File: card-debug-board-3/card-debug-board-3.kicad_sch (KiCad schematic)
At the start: 98 parts, among them J1 USB4105-GF-A, J2 USB4105-GF-A, J3 Conn_01x05, J4 5040501291, J5 2-1734592-0, Q1 PMV450ENEAR, Q2 PMV450ENEAR, Q3 NTR4101P, SW1 B3F-1000, SW2 PCM13SMTR, SW3 B3F-1000, SW4 SW_DIP_x01, U1 MIC5205-3.3YM5, U2 W25Q16JVSS, U3 RP2040, U4 74AUP1G17, U5 74AUP1G17, U6 IP4234CZ6,125, U7 IP4234CZ6,125, Y1 12 MHz

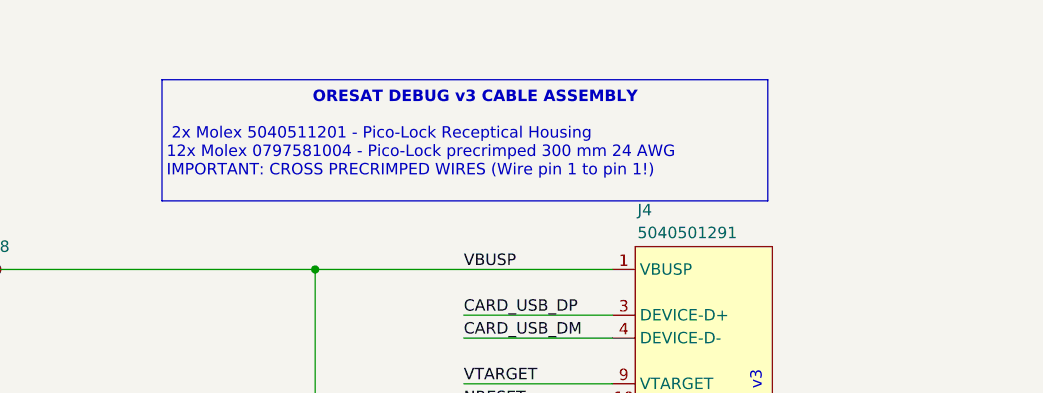
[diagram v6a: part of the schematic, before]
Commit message: Fixed note on card debug v3 cable assembly - it was wrong!
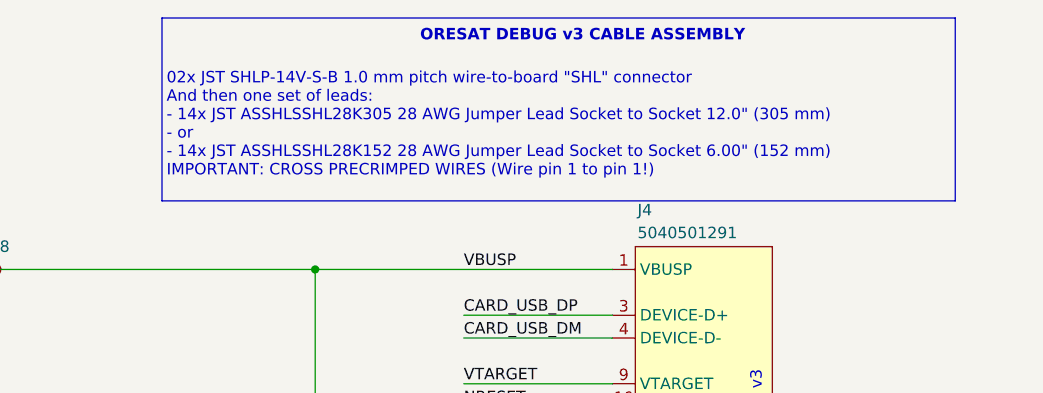
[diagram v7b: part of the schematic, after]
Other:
- note added: "02x JST SHLP-14V-S-B 1.0 mm pitch wire-to-board "SHL" connector And then one set of leads: - 14x JST ASSHLSSHL28K305 28 AWG Jumper Lead Socket to Socket 12.0" (305 mm) - or - 14x JST ASSHLSSHL28K152 28 AWG Jumper Lead Socket to Socket 6.00" (152 mm) IMPORTANT: CROSS PRECRIMPED WIRES (Wire pin 1 to pin 1!)"
- note removed: "2x Molex 5040511201 - Pico-Lock Receptical Housing 12x Molex 0797581004 - Pico-Lock precrimped 300 mm 24 AWG IMPORTANT: CROSS PRECRIMPED WIRES (Wire pin 1 to pin 1!)"
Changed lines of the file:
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@@
 	)
 	(rectangle
-		(start 318.262 25.908)
-		(end 385.572 39.37)
+		(start 318.262 19.05)
+		(end 406.4 39.37)
 		(stroke
 			(width 0)
@@
 		)
 	)
-	(text " 2x Molex 5040511201 - Pico-Lock Receptical Housing\n12x Molex 0797581004 - Pico-Lock precrimped 300 mm 24 AWG\nIMPORTANT: CROSS PRECRIMPED WIRES (Wire pin 1 to pin 1!)"
+	(text "02x JST SHLP-14V-S-B 1.0 mm pitch wire-to-board \"SHL\" connector\nAnd then one set of leads:\n- 14x JST ASSHLSSHL28K305 28 AWG Jumper Lead Socket to Socket 12.0\" (305 mm)\n- or \n- 14x JST ASSHLSSHL28K152 28 AWG Jumper Lead Socket to Socket 6.00\" (152 mm)\nIMPORTANT: CROSS PRECRIMPED WIRES (Wire pin 1 to pin 1!)"
 		(exclude_from_sim no)
 		(at 318.77 36.83 0)
@@
 	(text "ORESAT DEBUG v3 CABLE ASSEMBLY"
 		(exclude_from_sim no)
-		(at 353.06 27.94 0)
+		(at 364.998 21.082 0)
 		(effects
 			(font

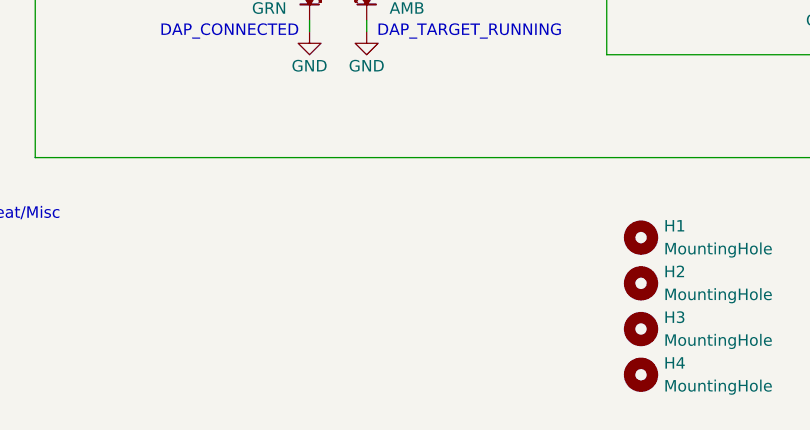
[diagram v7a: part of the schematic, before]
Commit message: Card Debug Board v3.2
Fixed SW2 through-holes which have never been right, added fiducials, added makefile and readmes.
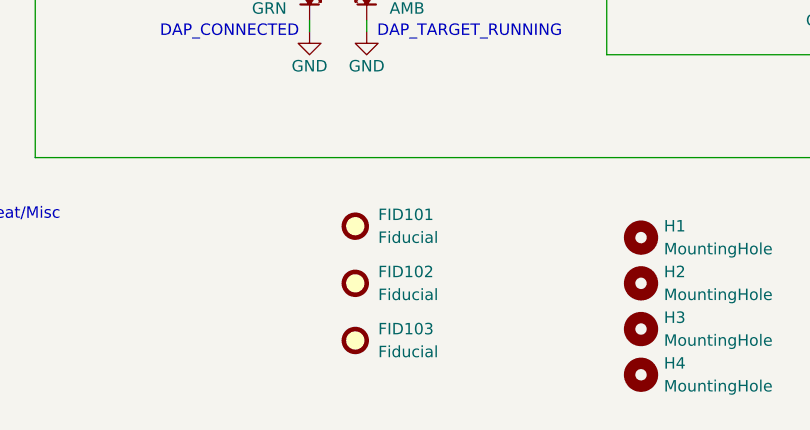
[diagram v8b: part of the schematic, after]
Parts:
- added FID101, FID102, FID103: Fiducial, Fiducial:Fiducial_0.5mm_Mask1mm, symbol Mechanical:Fiducial
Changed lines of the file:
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@@
 	(title_block
 		(title "Card Debug Board")
-		(date "2026-02-08")
-		(rev "3.1")
+		(date "2026-03-11")
+		(rev "3.2")
 		(company "Portland State Aerospace Society")
 	)
@@
 	)
 	(symbol
+		(lib_id "Mechanical:Fiducial")
+		(at 215.9 242.57 0)
+		(unit 1)
+		(exclude_from_sim no)
+		(in_bom no)
+		(on_board yes)
+		(dnp no)
+		(fields_autoplaced yes)
+		(property "Reference" "FID101"
+			(at 218.44 241.2999 0)
+			(effects
+				(font
+					(size 1.27 1.27)
+				)
+				(justify left)
+			)
+		)
+		(property "Value" "Fiducial"
+			(at 218.44 243.8399 0)
+			(effects
+				(font
+					(size 1.27 1.27)
+				)
+				(justify left)
+			)
+		)
+		(property "Footprint" "Fiducial:Fiducial_0.5mm_Mask1mm"
+			(at 215.9 242.57 0)
+			(effects
+				(font
+					(size 1.27 1.27)
+				)
+				(hide yes)
+			)
+		)
+		(property "Datasheet" "~"
+			(at 215.9 242.57 0)
+			(effects
+				(font
+					(size 1.27 1.27)
+				)
+				(hide yes)
+			)
+		)
+		(property "Description" "Fiducial Marker"
+			(at 215.9 242.57 0)
+			(effects
+				(font
+					(size 1.27 1.27)
+				)
+				(hide yes)
+			)
+		)
+		(instances
+			(project ""
+				(path "/6ec99451-f949-47af-a175-ad55f6cf8202"
+					(reference "FID101")
+					(unit 1)
+				)
+			)
+		)
+	)
+	(symbol
 		(lib_id "power:GND")
 		(at 71.12 194.31 0)
@@
 	)
 	(symbol
+		(lib_id "Mechanical:Fiducial")
+		(at 215.9 255.27 0)
+		(unit 1)
+		(exclude_from_sim no)
+		(in_bom no)
+		(on_board yes)
+		(dnp no)
+		(fields_autoplaced yes)
+		(property "Reference" "FID103"
+			(at 218.44 253.9999 0)
+			(effects
+				(font
+					(size 1.27 1.27)
+				)
+				(justify left)
+			)
+		)
+		(property "Value" "Fiducial"
+			(at 218.44 256.5399 0)
+			(effects
+				(font
+					(size 1.27 1.27)
+				)
+				(justify left)
+			)
+		)
+		(property "Footprint" "Fiducial:Fiducial_0.5mm_Mask1mm"
+			(at 215.9 255.27 0)
+			(effects
+				(font
+					(size 1.27 1.27)
+				)
+				(hide yes)
+			)
+		)
+		(property "Datasheet" "~"
+			(at 215.9 255.27 0)
+			(effects
+				(font
+					(size 1.27 1.27)
+				)
+				(hide yes)
+			)
+		)
+		(property "Description" "Fiducial Marker"
+			(at 215.9 255.27 0)
+			(effects
+				(font
+					(size 1.27 1.27)
+				)
+				(hide yes)
+			)
+		)
+		(instances
+			(project ""
+				(path "/6ec99451-f949-47af-a175-ad55f6cf8202"
+					(reference "FID103")
+					(unit 1)
+				)
+			)
+		)
+	)
+	(symbol
 		(lib_id "Mechanical:MountingHole")
 		(at 247.65 254 0)
@@
 					(unit 1)
 				)
+			)
+		)
+	)
+	(symbol
+		(lib_id "Mechanical:Fiducial")
+		(at 215.9 248.92 0)
+		(unit 1)
+		(exclude_from_sim no)
+		(in_bom no)
+		(on_board yes)
+		(dnp no)
+		(fields_autoplaced yes)
+		(property "Reference" "FID102"
+			(at 218.44 247.6499 0)
+			(effects
+				(font
+					(size 1.27 1.27)
+				)
+				(justify left)
+			)
+		)
+		(property "Value" "Fiducial"
+			(at 218.44 250.1899 0)
+			(effects
+				(font
+					(size 1.27 1.27)
+				)
+				(justify left)
+			)
+		)
+		(property "Footprint" "Fiducial:Fiducial_0.5mm_Mask1mm"
+			(at 215.9 248.92 0)
+			(effects
+				(font
+					(size 1.27 1.27)
+				)
+				(hide yes)
+			)
+		)
+		(property "Datasheet" "~"
+			(at 215.9 248.92 0)
+			(effects
+				(font
+					(size 1.27 1.27)
+				)
+				(hide yes)
+			)
+		)
+		(property "Description" "Fiducial Marker"
+			(at 215.9 248.92 0)
+			(effects
+				(font
+					(size 1.27 1.27)
+				)
+				(hide yes)
+			)
+		)
+		(instances
+			(project ""
+				(path "/6ec99451-f949-47af-a175-ad55f6cf8202"
+					(reference "FID102")
+					(unit 1)
+				)
